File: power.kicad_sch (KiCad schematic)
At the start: 0 parts

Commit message: updates to power, ferrites etc
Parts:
- added U?: LM1086CS-5.0/NOPB, symbol tbc:LM1086CS-5.0/NOPB
- added U?: LM1086CS-3.3/NOPB, symbol tbc:LM1086CS-3.3/NOPB
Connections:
- new net: U?.3 (INPUT), U?.3 (INPUT)
- new net +3V3: U?.2 (OUT), U?.TAB (OUT)
- new net +5V: U?.2 (OUT), U?.TAB (OUT)
- new net GND: U?.1 (ADJ/GND), U?.1 (ADJ/GND)
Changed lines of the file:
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@@
 (kicad_sch (version 20230121) (generator eeschema)
   (paper "A4")
+  (junction (at 181.61 114.3) (diameter 0) (color 0 0 0 0)
+  )
+  (junction (at 181.61 78.74) (diameter 0) (color 0 0 0 0)
+  )
+  (junction (at 130.81 80.01) (diameter 0) (color 0 0 0 0)
+  )
+  (wire (pts (xy 180.34 114.3) (xy 181.61 114.3))
+    (stroke (width 0) (type default))
+  )
+  (wire (pts (xy 180.34 81.28) (xy 181.61 81.28))
+    (stroke (width 0) (type default))
+  )
+  (wire (pts (xy 181.61 78.74) (xy 193.04 78.74))
+    (stroke (width 0) (type default))
+  )
+  (wire (pts (xy 180.34 78.74) (xy 181.61 78.74))
+    (stroke (width 0) (type default))
+  )
+  (wire (pts (xy 130.81 80.01) (xy 154.94 80.01))
+    (stroke (width 0) (type default))
+  )
+  (wire (pts (xy 181.61 114.3) (xy 193.04 114.3))
+    (stroke (width 0) (type default))
+  )
+  (wire (pts (xy 127 80.01) (xy 130.81 80.01))
+    (stroke (width 0) (type default))
+  )
+  (wire (pts (xy 130.81 115.57) (xy 130.81 80.01))
+    (stroke (width 0) (type default))
+  )
+  (wire (pts (xy 167.64 123.19) (xy 167.64 124.46))
+    (stroke (width 0) (type default))
+  )
+  (wire (pts (xy 181.61 78.74) (xy 181.61 81.28))
+    (stroke (width 0) (type default))
+  )
+  (wire (pts (xy 180.34 116.84) (xy 181.61 116.84))
+    (stroke (width 0) (type default))
+  )
+  (wire (pts (xy 154.94 115.57) (xy 130.81 115.57))
+    (stroke (width 0) (type default))
+  )
+  (wire (pts (xy 167.64 87.63) (xy 167.64 88.9))
+    (stroke (width 0) (type default))
+  )
+  (wire (pts (xy 181.61 114.3) (xy 181.61 116.84))
+    (stroke (width 0) (type default))
+  )
+  (label "+3V3" (at 193.04 78.74 180) (fields_autoplaced)
+    (effects (font (size 1.27 1.27)) (justify right bottom))
+  )
+  (label "+5V" (at 193.04 114.3 180) (fields_autoplaced)
+    (effects (font (size 1.27 1.27)) (justify right bottom))
+  )
+  (symbol (lib_id "tbc:GND") (at 167.64 124.46 0) (unit 1)
+    (in_bom yes) (on_board yes) (dnp no) (fields_autoplaced)
+    (property "Reference" "#PWR030" (at 167.64 130.81 0)
+      (effects (font (size 1.27 1.27)) hide)
+    )
+    (property "Value" "GND" (at 167.64 129.54 0)
+      (effects (font (size 1.27 1.27)))
+    )
+    (property "Footprint" "" (at 167.64 124.46 0)
+      (effects (font (size 1.27 1.27)) hide)
+    )
+    (property "Datasheet" "" (at 167.64 124.46 0)
+      (effects (font (size 1.27 1.27)) hide)
+    )
+    (pin "1")
+    (instances
+      (project "tbc"
+        (path "/9df71e53-7941-4fd3-a17d-93619e4e3e02/62085b71-69bf-4103-9630-c632803684fd"
+          (reference "#PWR030") (unit 1)
+        )
+      )
+    )
+  )
+  (symbol (lib_id "tbc:LM1086CS-5.0/NOPB") (at 167.64 115.57 0) (unit 1)
+    (in_bom yes) (on_board yes) (dnp no)
+    (property "Reference" "U?" (at 160.02 109.22 0)
+      (effects (font (size 1.27 1.27)))
+    )
+    (property "Value" "LM1086CS-5.0/NOPB" (at 180.34 121.92 0)
+      (effects (font (size 1.27 1.27)))
+    )
+    (property "Footprint" "" (at 156.21 121.92 0)
+      (effects (font (size 1.27 1.27)) hide)
+    )
+    (property "Datasheet" "https://www.ti.com/lit/gpn/lm1086" (at 168.91 133.35 0) (show_name)
+      (effects (font (size 1.27 1.27)) hide)
+    )
+    (property "Mouser" "926-LM1086CS-5.0NOPB" (at 166.37 135.89 0) (show_name)
+      (effects (font (size 1.27 1.27)) hide)
+    )
+    (pin "2")
+    (pin "1")
+    (pin "3")
+    (pin "TAB")
+    (instances
+      (project "tbc"
+        (path "/9df71e53-7941-4fd3-a17d-93619e4e3e02/62085b71-69bf-4103-9630-c632803684fd"
+          (reference "U?") (unit 1)
+        )
+      )
+    )
+  )
+  (symbol (lib_id "tbc:GND") (at 167.64 88.9 0) (unit 1)
+    (in_bom yes) (on_board yes) (dnp no) (fields_autoplaced)
+    (property "Reference" "#PWR029" (at 167.64 95.25 0)
+      (effects (font (size 1.27 1.27)) hide)
+    )
+    (property "Value" "GND" (at 167.64 93.98 0)
+      (effects (font (size 1.27 1.27)))
+    )
+    (property "Footprint" "" (at 167.64 88.9 0)
+      (effects (font (size 1.27 1.27)) hide)
+    )
+    (property "Datasheet" "" (at 167.64 88.9 0)
+      (effects (font (size 1.27 1.27)) hide)
+    )
+    (pin "1")
+    (instances
+      (project "tbc"
+        (path "/9df71e53-7941-4fd3-a17d-93619e4e3e02/62085b71-69bf-4103-9630-c632803684fd"
+          (reference "#PWR029") (unit 1)
+        )
+      )
+    )
+  )
+  (symbol (lib_id "tbc:LM1086CS-3.3/NOPB") (at 167.64 80.01 0) (unit 1)
+    (in_bom yes) (on_board yes) (dnp no)
+    (property "Reference" "U?" (at 160.02 73.66 0)
+      (effects (font (size 1.27 1.27)))
+    )
+    (property "Value" "LM1086CS-3.3/NOPB" (at 180.34 86.36 0)
+      (effects (font (size 1.27 1.27)))
+    )
+    (property "Footprint" "" (at 156.21 86.36 0)
+      (effects (font (size 1.27 1.27)) hide)
+    )
+    (property "Datasheet" "https://www.ti.com/lit/gpn/lm1086" (at 168.91 97.79 0) (show_name)
+      (effects (font (size 1.27 1.27)) hide)
+    )
+    (property "Mouser" "926-LM1086CSX3.3NOPB" (at 166.37 100.33 0) (show_name)
+      (effects (font (size 1.27 1.27)) hide)
+    )
+    (pin "TAB")
+    (pin "3")
+    (pin "2")
+    (pin "1")
+    (instances
+      (project "tbc"
+        (path "/9df71e53-7941-4fd3-a17d-93619e4e3e02/62085b71-69bf-4103-9630-c632803684fd"
+          (reference "U?") (unit 1)
+        )
+      )
+    )
+  )
 )

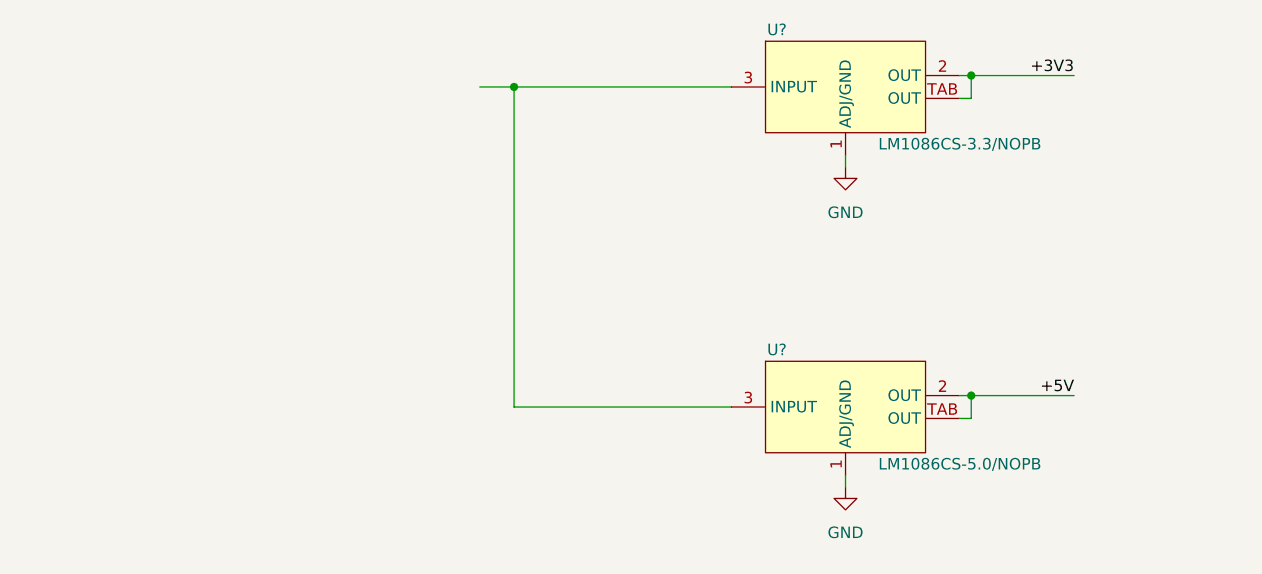
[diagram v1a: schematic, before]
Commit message: added encoder to schematic
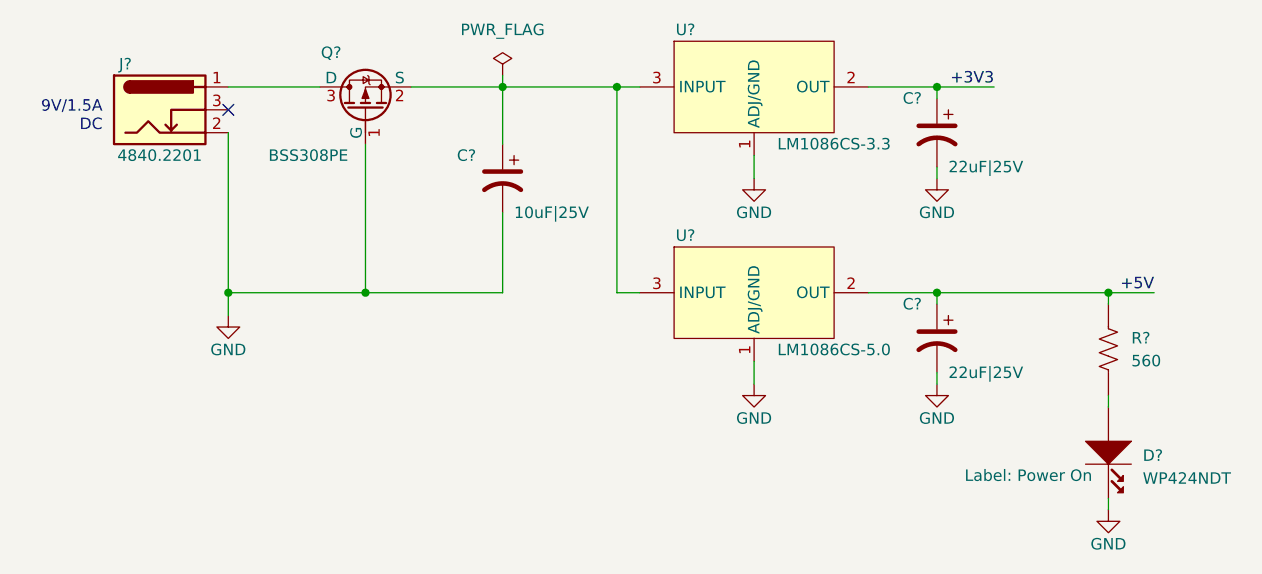
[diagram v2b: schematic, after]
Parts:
- removed U?: LM1086CS-5.0/NOPB, symbol tbc:LM1086CS-5.0/NOPB
- removed U?: LM1086CS-3.3/NOPB, symbol tbc:LM1086CS-3.3/NOPB
- added C? (x2): 22uF|25V, symbol tbc:593D226X9025D2TE3
- added C?: 10uF|25V, symbol tbc:293D106X9025C2TE3
- added D?: WP424NDT, symbol tbc:WP424NDT
- added J?: 4840.2201, symbol tbc:4840.2201
- added Q?: BSS308PE, symbol tbc:BSS308PE
- added R?: 560, symbol tbc:RC0603FR-07560RL
- added U?: LM1086CS-3.3, symbol tbc:LM1086CS-3.3
- added U?: LM1086CS-5.0, symbol tbc:LM1086CS-5.0
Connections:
- net +3V3: now also C?.1, U?.2 (OUT)
- net +5V: now also C?.1, R?.2, U?.2 (OUT)
- net GND: now also C?.2, C?.2, C?.2, D?.1 (Cathode), J?.2, Q?.1 (G), U?.1 (ADJ/GND), U?.1 (ADJ/GND)
- new net: C?.1, Q?.2 (S), U?.3 (INPUT), U?.3 (INPUT)
- new net: D?.2 (Anode), R?.1
- new net: J?.1, Q?.3 (D)
- no-connect marks 0 -> 1
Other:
- note added: "9V/1.5A DC"
